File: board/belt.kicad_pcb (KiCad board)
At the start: 2 copper layers, 48.9 x 75.5 mm, 33 parts, among them J1 USB_B_Micro, J2 USB_B_Micro, J3 USB_B_Micro, J4 USB_B_Micro, P1 3352T-1-103LF, P2 3352T-1-103LF, Q1 BSS138, Q2 BSS138, SW1 SW_DPDT, SW2 SW_Push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

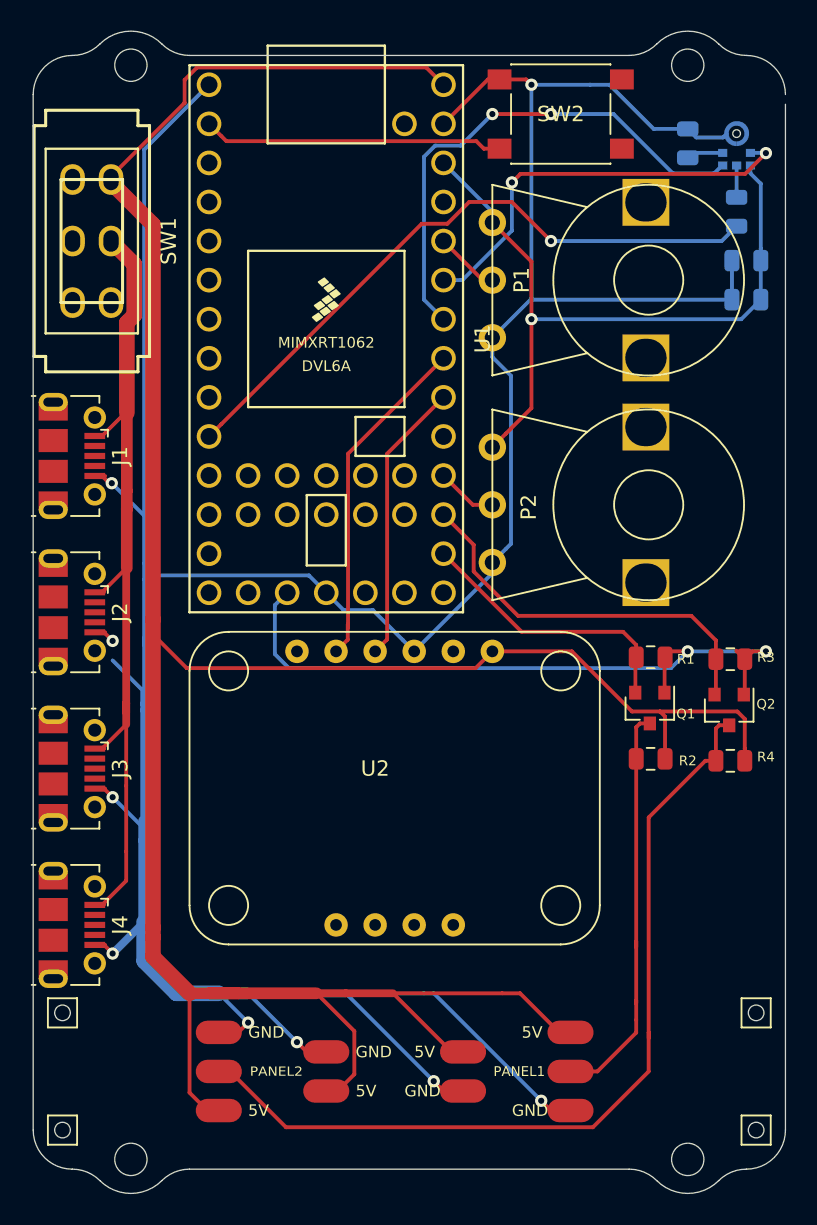
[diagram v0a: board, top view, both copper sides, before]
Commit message: narrow board width slightly and center led ports on the bottom
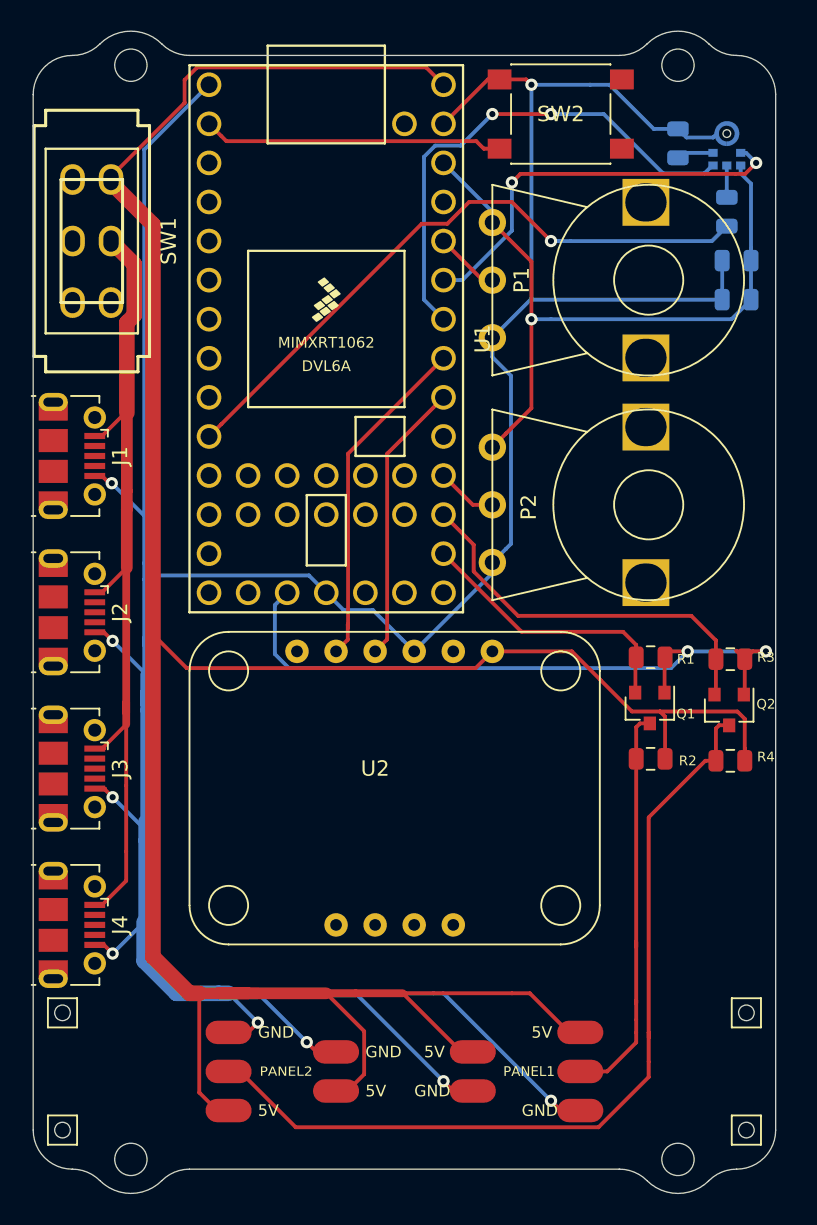
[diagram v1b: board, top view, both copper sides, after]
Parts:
- moved C1 0.64 mm to (165.1, 81.9)
- moved C2 0.64 mm to (165.1, 84.5)
- moved PANEL2 0.64 mm to (132.1, 134.6)
- moved PANEL_PWR1 0.64 mm to (148.0, 134.6)
- moved R5 0.64 mm to (161.3, 74.3)
- moved REF** 0.64 mm to (161.3, 69.2)
- moved REF** 0.64 mm to (161.3, 140.3)
- moved MK1 0.63 mm to (164.5, 73.7)
- moved PANEL1 0.63 mm to (154.9, 134.6)
- moved PANEL_PWR2 0.63 mm to (139.1, 134.6)
- moved R6 0.63 mm to (164.5, 78.7)
- moved REF** 0.63 mm to (165.7, 130.8)
- moved REF** 0.63 mm to (165.7, 138.4)
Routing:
- net GND: track 231.9 -> 229.4 mm
- net VBUS: track 56.6 -> 55.6 mm
- net VDD: track 183.6 -> 184.3 mm
- net +3.3VA: track 46.3 -> 45.7 mm
- net /MIC_LRCLK: track 33.5 -> 32.8 mm
- net /MIC_BCLK: track 27.2 -> 26.6 mm
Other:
- board size 48.9 x 75.5 mm -> 48.3 x 75.5 mm

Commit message: digikey was out of the DPDT switch I was going to use, so replace with a smaller (better?) one; shrink board vertically slightly in response
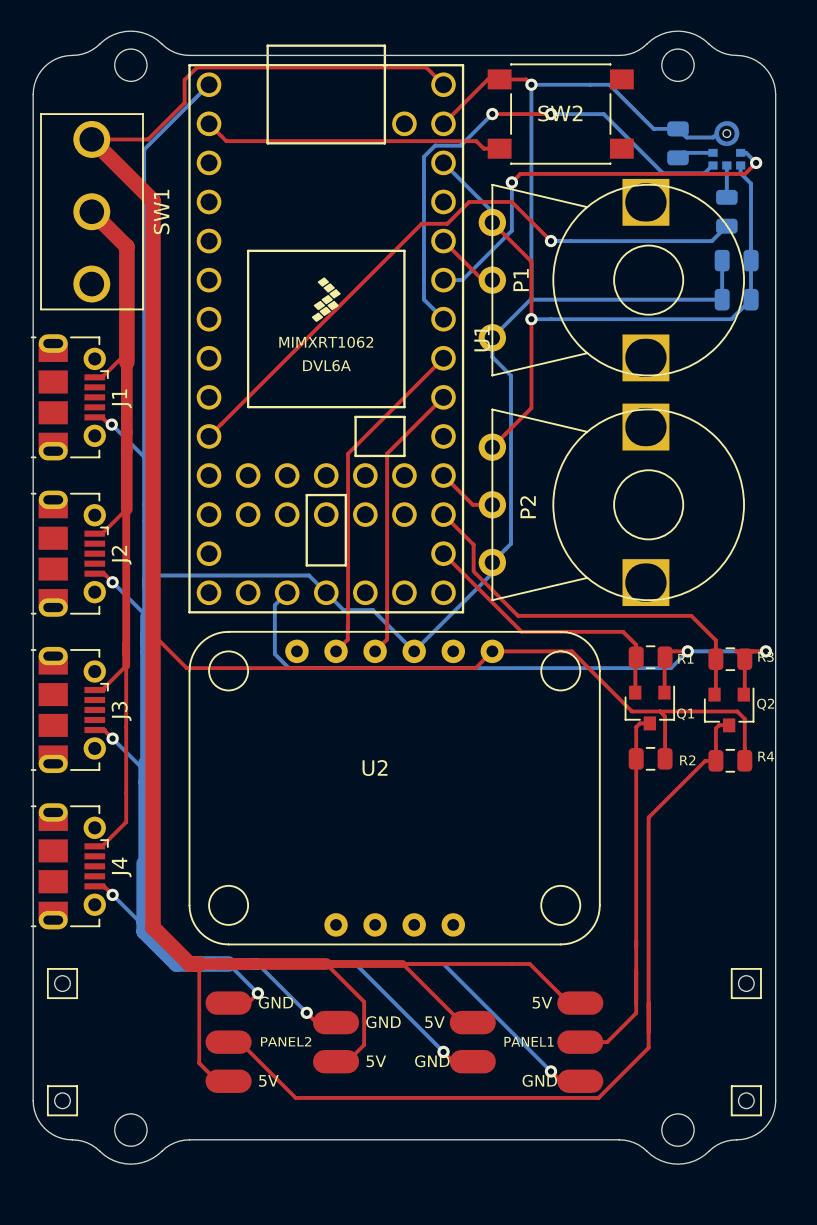
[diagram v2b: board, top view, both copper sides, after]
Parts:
- SW1: value SW_DPDT -> SW_SPDT; footprint engstad:slide-switch-MFS201N-9-Z -> Extra SMD Components:Button_Switch_SPDT_GH36P010001
- moved J2 3.81 mm to (121.9, 101.0)
- moved J3 3.81 mm to (121.9, 111.1)
- moved J4 3.81 mm to (121.9, 121.3)
- moved J1 3.81 mm to (121.9, 90.8)
- moved PANEL1 1.91 mm to (154.9, 132.7)
- moved PANEL2 1.91 mm to (132.1, 132.7)
- moved PANEL_PWR1 1.91 mm to (148.0, 132.7)
- moved PANEL_PWR2 1.91 mm to (139.1, 132.7)
- moved REF** 1.91 mm to (165.7, 128.9)
- moved REF** 1.91 mm to (165.7, 136.5)
- moved REF** 1.91 mm to (121.3, 136.5)
- moved REF** 1.91 mm to (121.3, 128.9)
- moved REF** 1.91 mm to (125.7, 138.4)
- moved REF** 1.91 mm to (161.3, 138.4)
- moved SW1 1.91 mm to (123.2, 78.7)
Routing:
- net GND: track 229.4 -> 226.6 mm
- net VBUS: track 55.6 -> 53.8 mm
- net VDD: track 184.3 -> 185.4 mm
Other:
- board size 48.3 x 75.5 mm -> 48.3 x 73.6 mm

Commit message: switch 10K resistors to 0603 package (being ambitious and buying in bulk); fix layout for new package
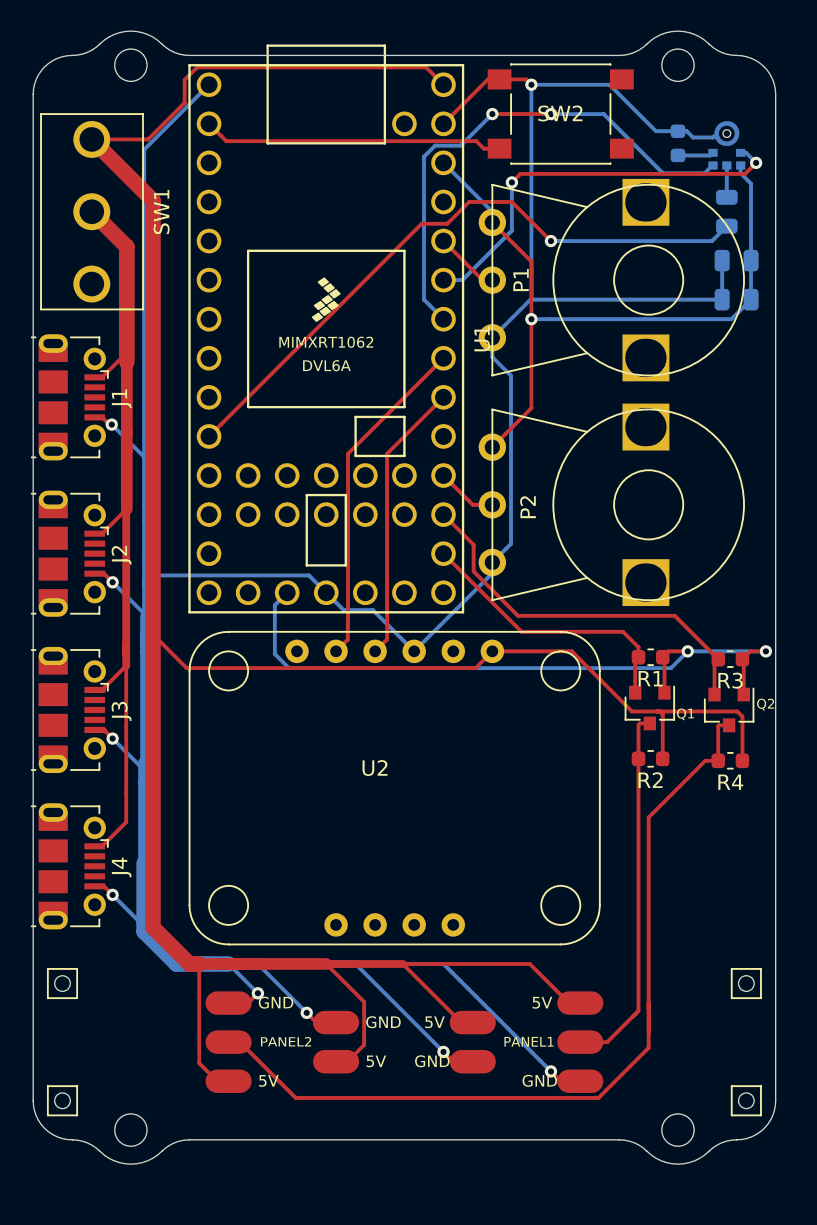
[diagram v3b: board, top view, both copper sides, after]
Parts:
- R1, R2, R3, R4, R5: footprint Resistor_SMD:R_0805_2012Metric -> Resistor_SMD:R_0603_1608Metric
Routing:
- net Net-(PANEL1-Pad2): track 26.5 -> 24.3 mm
- net /DATA2: track 25.8 -> 25.2 mm
- net +3V3: track 45.8 -> 45.3 mm

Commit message: fix schematic symbol which was using old POT symbol
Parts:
- P1, P2: value 3352T-1-103LF -> 10K
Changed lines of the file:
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@@
       (effects (font (size 1 1) (thickness 0.15)))
     )
-    (fp_text value 3352T-1-103LF (at 0.1016 -6.477 90) (layer F.Fab)
+    (fp_text value 10K (at 0.1016 -6.477 90) (layer F.Fab)
       (effects (font (size 1 1) (thickness 0.15)))
     )
@@
       (effects (font (size 1 1) (thickness 0.15)))
     )
-    (fp_text value 3352T-1-103LF (at 0.1016 -6.477 90) (layer F.Fab)
+    (fp_text value 10K (at 0.1016 -6.477 90) (layer F.Fab)
       (effects (font (size 1 1) (thickness 0.15)))
     )
@@
   (segment (start 166.0375 84.455) (end 164.7675 85.725) (width 0.25) (layer B.Cu) (net 63))
   (segment (start 149.225 78.74) (end 149.225 79.4385) (width 0.25) (layer B.Cu) (net 63))
-  (segment (start 146.05 75.565) (end 149.225 78.74) (width 0.25) (layer B.Cu) (net 63))
   (segment (start 151.765 91.5035) (end 150.113999 93.154501) (width 0.25) (layer F.Cu) (net 63))
   (segment (start 151.765 81.9785) (end 151.765 91.5035) (width 0.25) (layer F.Cu) (net 63))
-  (segment (start 149.225 79.4385) (end 151.765 81.9785) (width 0.25) (layer F.Cu) (net 63))
   (segment (start 150.113999 93.154501) (end 149.225 94.0435) (width 0.25) (layer F.Cu) (net 63))
   (via (at 151.765 85.725) (size 0.8) (drill 0.4) (layers F.Cu B.Cu) (net 63))
   (segment (start 151.765 85.725) (end 153.035 85.725) (width 0.25) (layer B.Cu) (net 63))
   (segment (start 164.7675 85.725) (end 153.035 85.725) (width 0.25) (layer B.Cu) (net 63))
+  (segment (start 149.225 79.4385) (end 151.765 81.9785) (width 0.25) (layer F.Cu) (net 63))
+  (segment (start 146.05 75.565) (end 149.225 78.74) (width 0.25) (layer B.Cu) (net 63))
   (segment (start 151.048601 76.281399) (end 150.495 76.835) (width 0.25) (layer F.Cu) (net 64))
   (via (at 150.495 76.835) (size 0.8) (drill 0.4) (layers F.Cu B.Cu) (net 64))

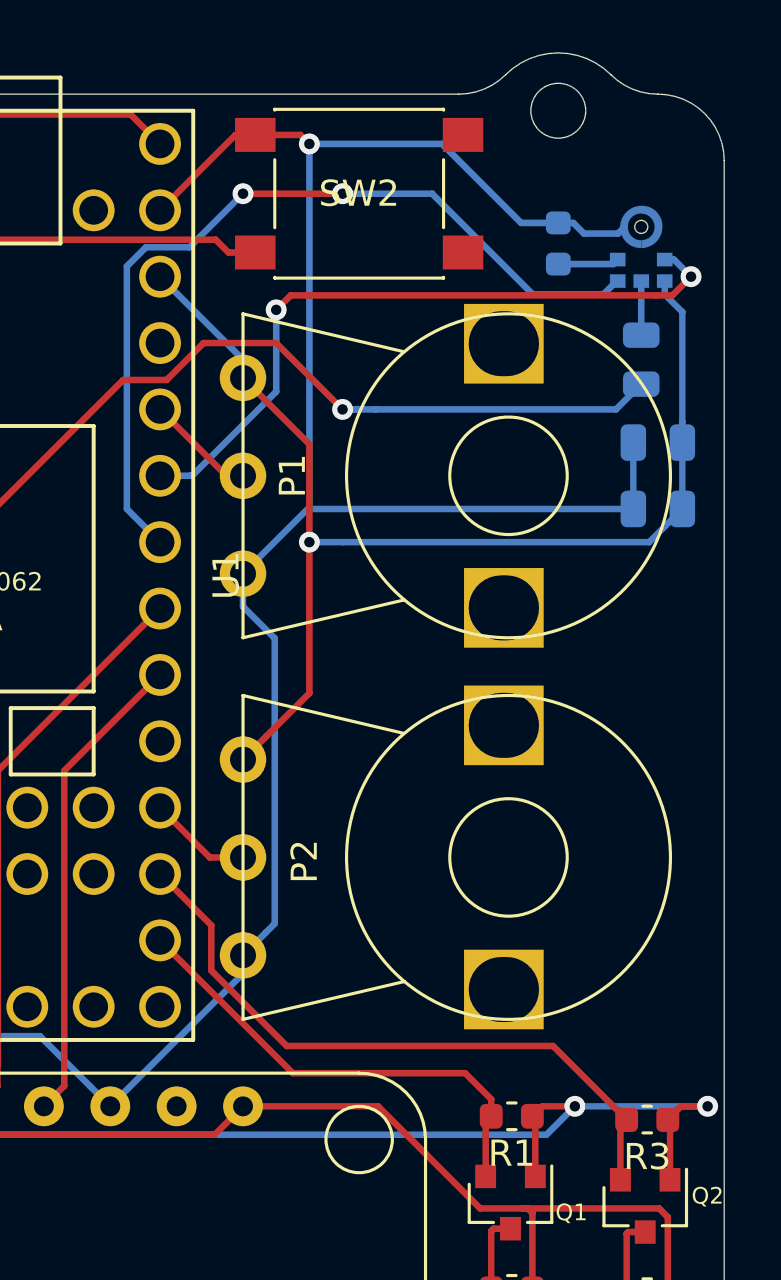
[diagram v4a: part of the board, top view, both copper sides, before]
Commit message: scoot pots apart to sorta be able to fit plastic tops
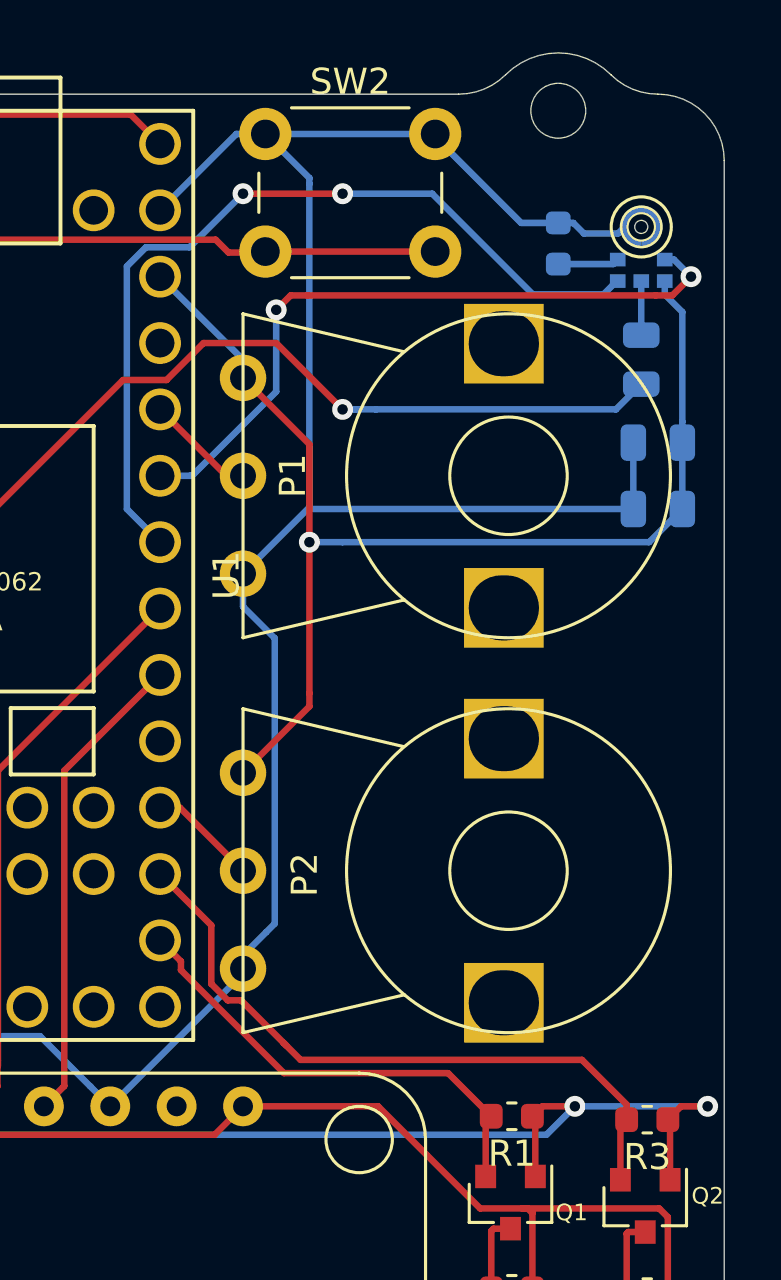
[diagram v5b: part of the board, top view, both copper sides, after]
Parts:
- SW2: footprint Button_Switch_SMD:SW_Push_1P1T_NO_6x6mm_H9.5mm -> Button_Switch_THT:SW_PUSH_6mm_H5mm
- moved SW2 4.26 mm to (150.1, 70.1)
- moved P2 0.51 mm to (149.2, 98.3)
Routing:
- net /BUTTON: track 19.6 -> 26.1 mm
- net /DATA2: track 25.2 -> 26.0 mm
- net GND: track 226.6 -> 227.3 mm, vias 9 -> 8
- net +3.3VA: track 45.7 -> 46.2 mm
